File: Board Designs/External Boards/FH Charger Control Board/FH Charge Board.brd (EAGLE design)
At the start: 76.6 x 50.8 mm, 15 parts, among them X1 CONNECTOR-2, X2 CONNECTOR-4, X3 CONNECTOR-2, X4 CONNECTOR-2

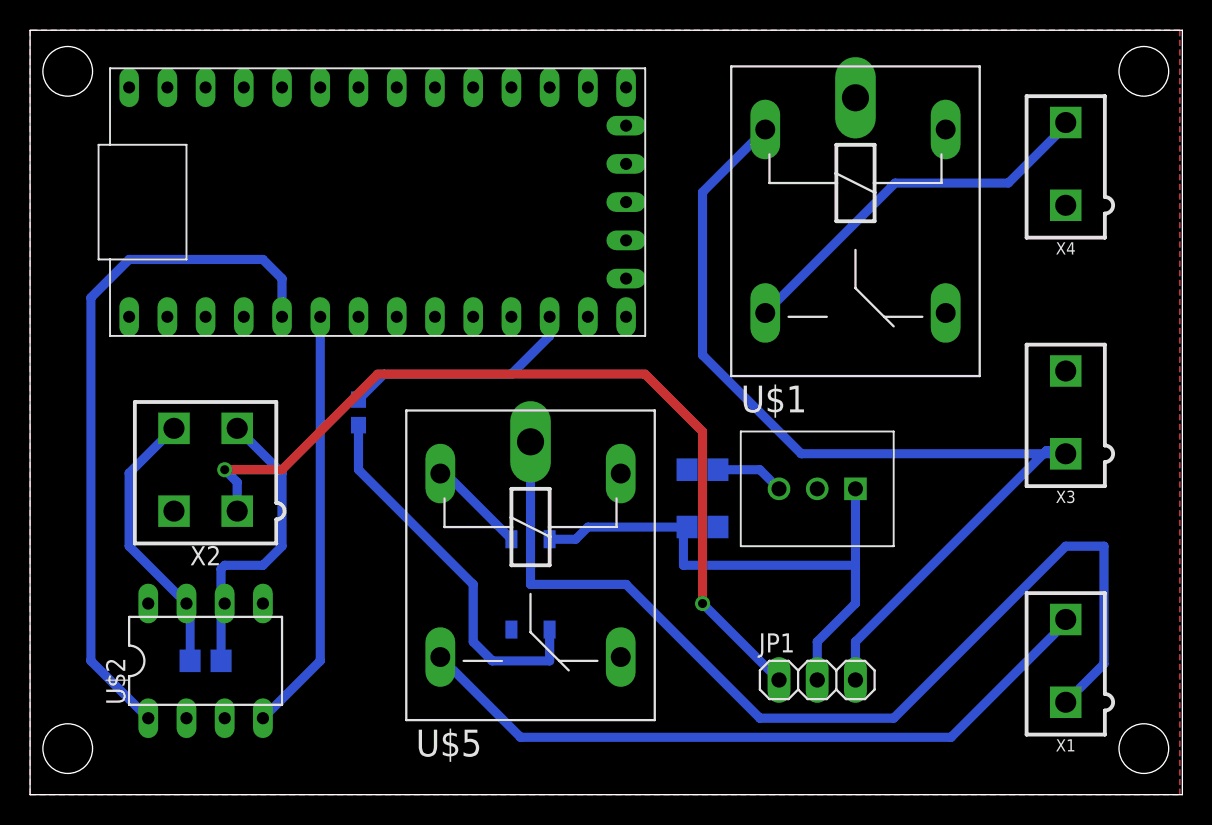
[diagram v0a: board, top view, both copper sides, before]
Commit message: Finalize BSPD Test Board, FH Charger Control Board for manufacturing; Update silkscreen, schematic spacing on HV Board; Move updates from rev4 to rev5 of Rear ECU; add silkscreen, rotate thermistor connectors on BMS Segment board
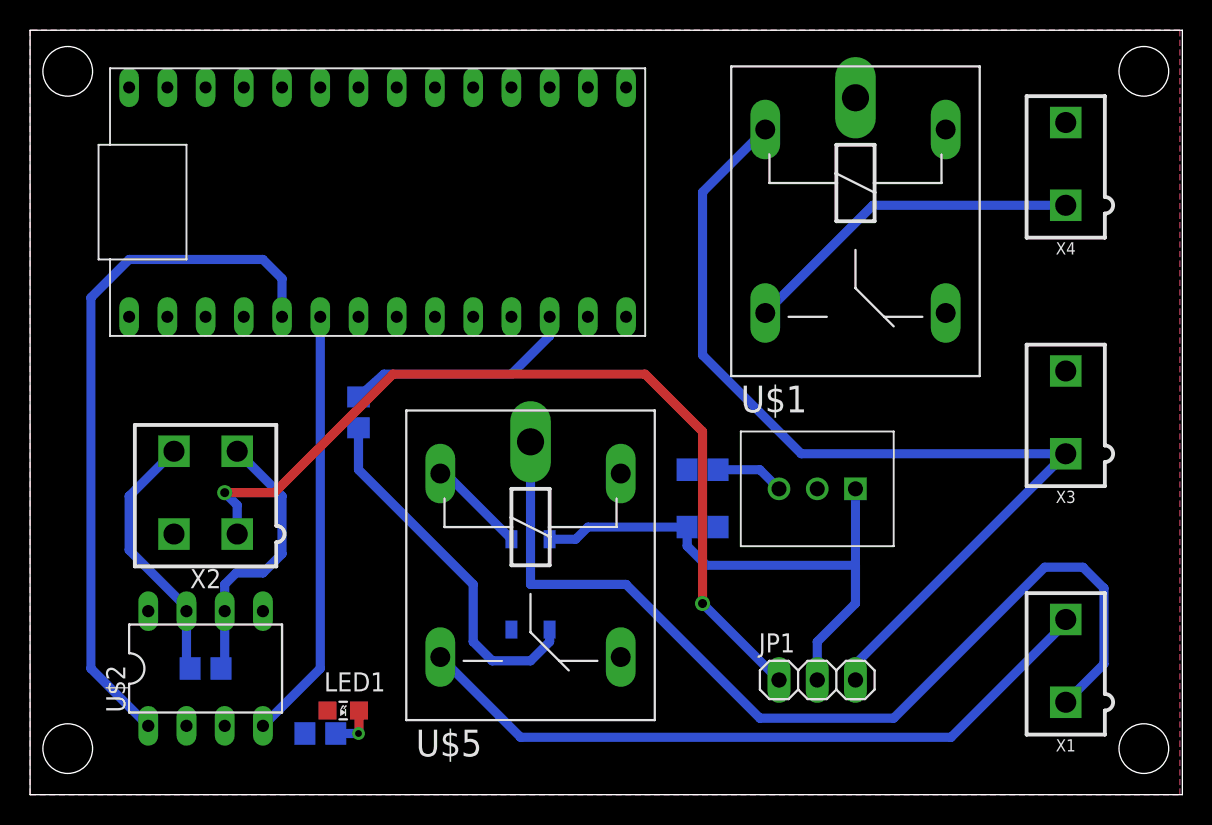
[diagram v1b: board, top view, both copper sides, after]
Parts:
- added LED1: PURPLE, HyTechDevices:LED-805
- added R3: 200, HyTechDevices:0805
- R1: value 2.5k -> 330; device HyTechDevices:0603-RES -> HyTechDevices:0805
- R2: value 120ohm -> 120
- U$3: value TEENSY_3.2_EXT -> TEENSY_3.2_SIMPLE; device HyTechDevices:TEENSY_3.2_EXT -> HyTechDevices:TEENSY_3.2_SIMPLE
- moved X2 1.52 mm to (10.2, 48.0)
- moved R2 0.51 mm to (10.2, 36.3)
- moved U$2 0.51 mm to (10.2, 36.3)
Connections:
- removed net N$15: U$1.S, X4.2
- new net N$1: U$1.S, X4.1
- new net N$2: LED1.C, R3.2
- net +5V: now also LED1.A
- net GND: now also R3.1, X4.2; no longer X4.1
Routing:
- net N$15: track 25.3 -> 0.00 mm
- net N$1: track 0.00 -> 22.9 mm
- net N$2: track 0.00 -> 3.05 mm, vias 0 -> 1
- net N$14: track 67.4 -> 64.6 mm
- net N$7: track 20.2 -> 18.4 mm
- net +12V: track 37.3 -> 36.2 mm
- net N$3: track 65.4 -> 64.4 mm
- net N$17: track 18.4 -> 17.3 mm
- net N$13: track 25.2 -> 24.3 mm
- net N$16: track 57.7 -> 58.3 mm
- net N$9: track 46.3 -> 46.8 mm
- net N$10: track 28.2 -> 28.8 mm
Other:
- board text added: "Charger Interlock"
- board text added: "HyTech 2018 FH Charger Controller Board rev0"
- board text added: "Power + CAN"
- board text added: "PowerSwitch Tail"
- board text added: "Shutdown Circuit"
- board text removed: "C:/Users/S. Kim/circuits-2017/EAGLE Supporting Files/Bitmaps for logos/GT_med.bmp"
- board text removed: "C:/Users/S. Kim/circuits-2017/EAGLE Supporting Files/Bitmaps for logos/HyTech_square.bmp"
- board text removed: "FH Charger Controller Board"

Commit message: Added labels and trace names on sch for quick reference
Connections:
- net N$10 renamed UC_CANRX
- net N$16 renamed PWR
- net N$17 renamed CANH
- net N$7 renamed CANL
- net N$9 renamed UC_CANTX
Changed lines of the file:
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@@
 <?xml version="1.0" encoding="utf-8"?>
 <!DOCTYPE eagle SYSTEM "eagle.dtd">
-<eagle version="8.4.1">
+<eagle version="8.3.1">
 <drawing>
 <settings>
@@
 <param name="dpMaxLengthDifference" value="10mm"/>
 <param name="dpGapFactor" value="2.5"/>
+<param name="checkGrid" value="0"/>
 <param name="checkAngle" value="0"/>
 <param name="checkFont" value="1"/>
 <param name="checkRestrict" value="1"/>
-<param name="checkStop" value="0"/>
 <param name="useDiameter" value="13"/>
 <param name="maxErrors" value="50"/>
@@
 <contactref element="R3" pad="1"/>
 </signal>
-<signal name="N$7">
+<signal name="CANL">
 <contactref element="U$2" pad="6"/>
 <contactref element="R2" pad="2"/>
@@
 <wire x1="11.43" y1="36.567" x2="11.185" y2="36.322" width="0.6096" layer="16"/>
 </signal>
-<signal name="N$10">
+<signal name="UC_CANRX">
 <contactref element="U$2" pad="4"/>
 <contactref element="U$3" pad="D4(CANRX)"/>
@@
 <wire x1="17.78" y1="36.322" x2="17.78" y2="59.69" width="0.6096" layer="16"/>
 </signal>
-<signal name="N$9">
+<signal name="UC_CANTX">
 <contactref element="U$2" pad="1"/>
 <contactref element="U$3" pad="D3(CANTX)"/>
@@
 <wire x1="53.34" y1="36.62" x2="53.34" y2="35.56" width="0.6096" layer="16"/>
 </signal>
-<signal name="N$16">
+<signal name="PWR">
 <contactref element="X2" pad="1"/>
 <contactref element="JP1" pad="1"/>
@@
 <wire x1="11.43" y1="48.006" x2="14.732" y2="48.006" width="0.6096" layer="1"/>
 </signal>
-<signal name="N$17">
+<signal name="CANH">
 <contactref element="R2" pad="1"/>
 <contactref element="U$2" pad="7"/>

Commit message: Added trace labels for quick reference
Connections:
- net N$1 renamed +IN
- net N$3 renamed SHUTDOWN_12V
- net PWR renamed POWER_CAN_12V
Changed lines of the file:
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@@
 <setting verticaltext="up"/>
 </settings>
-<grid distance="0.01" unitdist="inch" unit="inch" style="lines" multiple="1" display="yes" altdistance="5" altunitdist="mil" altunit="mm"/>
+<grid distance="0.01" unitdist="inch" unit="inch" style="lines" multiple="1" display="no" altdistance="5" altunitdist="mil" altunit="mm"/>
 <layers>
 <layer number="1" name="Top" color="4" fill="1" visible="yes" active="yes"/>
@@
 <wire x1="42.155" y1="44.459" x2="43.434" y2="43.18" width="0.6096" layer="16"/>
 </signal>
-<signal name="N$3">
+<signal name="SHUTDOWN_12V">
 <contactref element="U$1" pad="2"/>
 <contactref element="X3" pad="1"/>
@@
 <wire x1="53.34" y1="36.62" x2="53.34" y2="35.56" width="0.6096" layer="16"/>
 </signal>
-<signal name="PWR">
+<signal name="POWER_CAN_12V">
 <contactref element="X2" pad="1"/>
 <contactref element="JP1" pad="1"/>
@@
 <wire x1="8.89" y1="36.567" x2="9.135" y2="36.322" width="0.6096" layer="16"/>
 </signal>
-<signal name="N$1">
+<signal name="+IN">
 <contactref element="X4" pad="1"/>
 <contactref element="U$1" pad="S"/>
